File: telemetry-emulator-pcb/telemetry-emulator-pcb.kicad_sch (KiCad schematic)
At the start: 34 parts, among them J1 CAN_TERM, J2 ENABLE_RX, SW1 5V-3V3

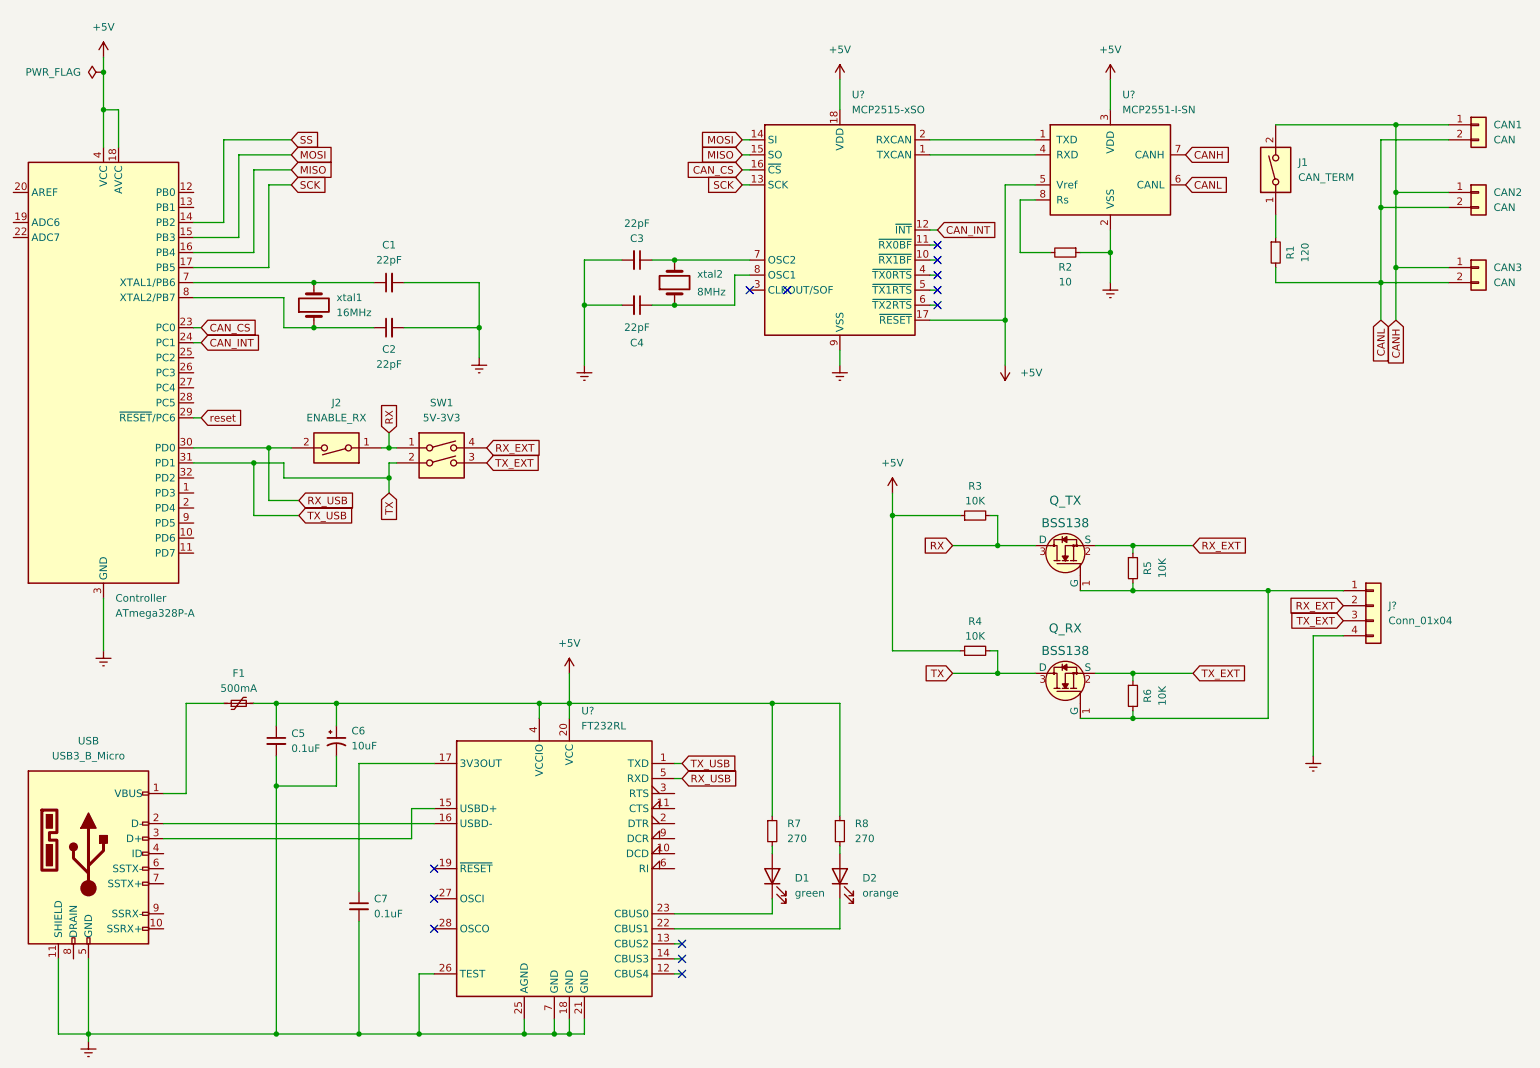
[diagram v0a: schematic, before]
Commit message: Connects rx/tx ext to UART connector
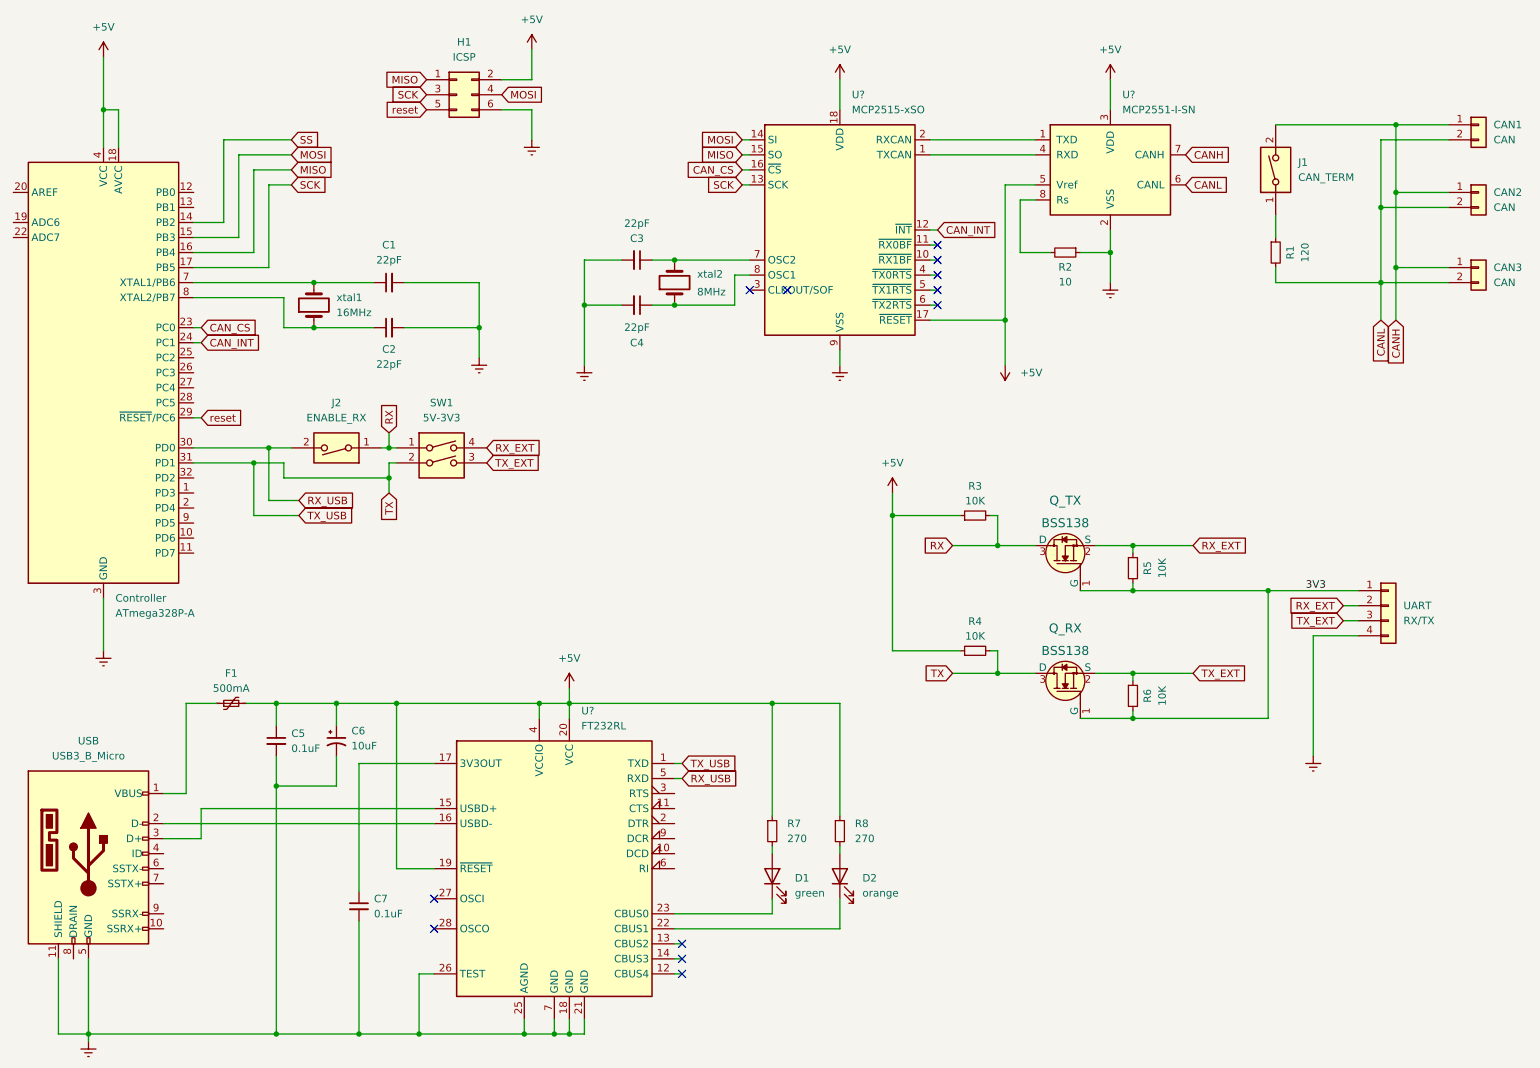
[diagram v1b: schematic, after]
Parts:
- added H1: ICSP, symbol Connector_Generic:Conn_02x03_Odd_Even
- UART: renamed from J?; value Conn_01x04 -> RX/TX
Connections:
- net +5V: now also U?.19 (~{RESET}), H1.2 (Pin_2)
- net Earth: now also H1.6 (Pin_6)
- net MISO: now also H1.1 (Pin_1)
- net MOSI: now also H1.4 (Pin_4)
- net SCK: now also H1.3 (Pin_3)
- net reset: now also H1.5 (Pin_5)
- net 3V3: now reaches Q_RX.1 (G), Q_TX.1 (G), R5.2, R6.2, UART.1 (Pin_1)
- no-connect marks 13 -> 12
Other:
- moved on the sheet: F1, UART
